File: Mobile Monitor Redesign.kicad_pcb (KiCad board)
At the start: 4 copper layers, 49 x 39.1 mm, 101 parts, among them J2 Conn_01x08_Pin, J3 Conn_01x08_Pin, J4 USB_C_Receptacle_USB2.0_16P, J7 Conn_01x05_Pin, J8 Conn_01x06_Socket, Q1 2N7002, Q2 AO3401A, Q3 BSS138, Q4 BSS138, Q5 AO3401A, Q6 2N7002, U1 ATmega2560-16A, U10 BQ27441DRZR-G1A, U11 TPL5010, U2 DS3232M, U5 XL4005, U6 IP5306, U7 CH340C, U8 FP6298XR, U9 AMS1117-3.3, Y2 Crystal

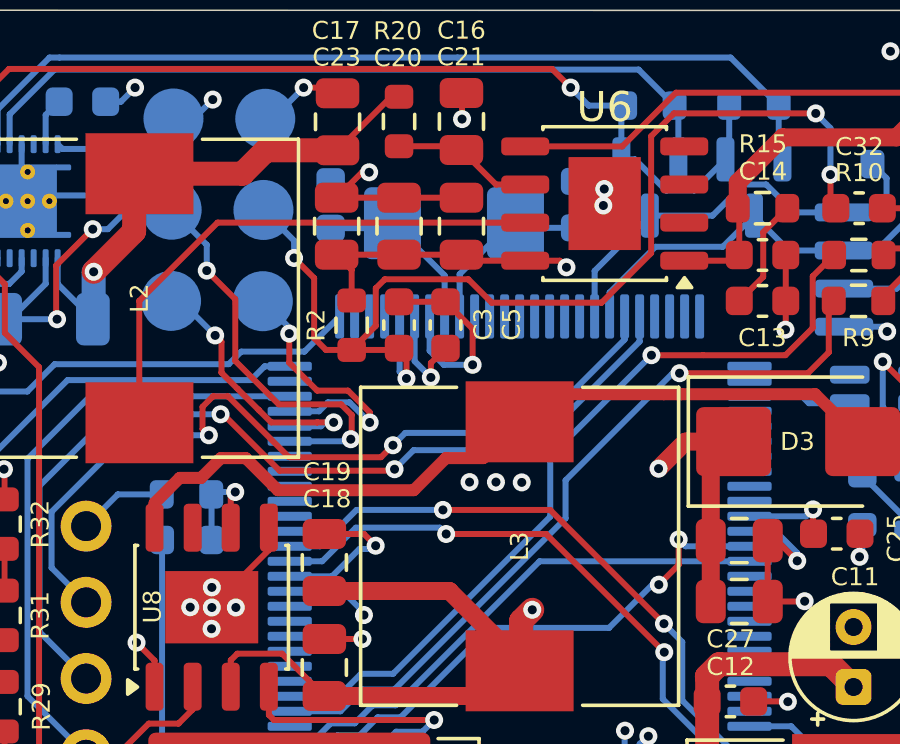
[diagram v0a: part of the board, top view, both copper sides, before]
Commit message: fixed some DRC errors and cleaned up routing
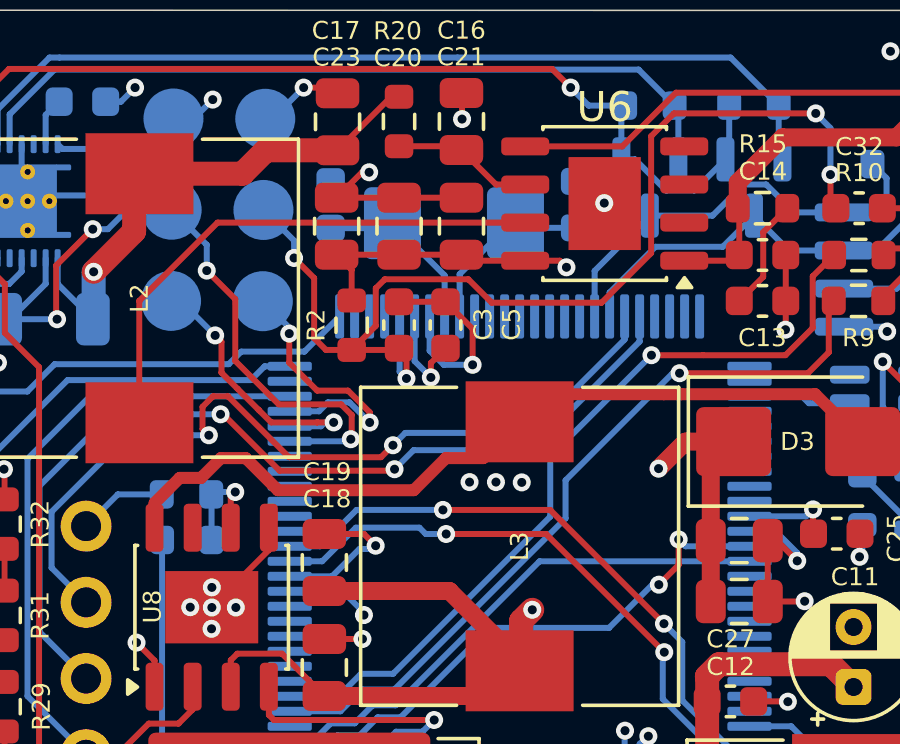
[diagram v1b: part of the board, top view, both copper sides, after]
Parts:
- renumbered 5V to gnd, 5V to vbat
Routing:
- net GND: track 102.5 -> 102.0 mm, vias 87 -> 86
